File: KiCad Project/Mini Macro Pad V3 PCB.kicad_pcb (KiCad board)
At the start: 2 copper layers, 65 x 65 mm, 59 parts, among them J1 USB_C_Receptacle_USB2.0_14P, SW1 SW_Push bootsel, SW10 SW_Push, SW11 SW_Push, SW12 SW_Push, SW13 SW_Push, SW14 SW_Push, SW15 SW_Push, SW16 SW_Push, SW17 SW_Push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

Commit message: more rough layout
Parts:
- C10, C9: moved to F.Cu
- C7: moved to B.Cu
- moved SW1 59.2 mm to (129.5, 119.0), turned to 180 degrees
- moved R1 52.2 mm to (131.5, 115.3), turned to 90 degrees
- moved C7 15.6 mm to (120.0, 98.4), turned to 0 degrees
- moved C10 14.0 mm to (124.0, 90.0), turned to -90 degrees
- moved Y1 13.8 mm to (119.0, 103.9)
- moved C9 13.6 mm to (118.5, 90.0), turned to 90 degrees
- moved C13 10.6 mm to (122.0, 103.9)
- moved R2 10.4 mm to (119.6, 101.2), turned to 180 degrees
- moved C12 10.3 mm to (116.0, 103.9), turned to -90 degrees
- moved C11 9.64 mm to (116.5, 90.0)
- moved C2 9.64 mm to (113.5, 97.0)
- moved C3 9.64 mm to (124.9, 93.5)
- moved C4 9.64 mm to (113.6, 93.5)
- moved C5 9.64 mm to (124.9, 97.0)
- moved C6 9.64 mm to (119.5, 89.9)
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
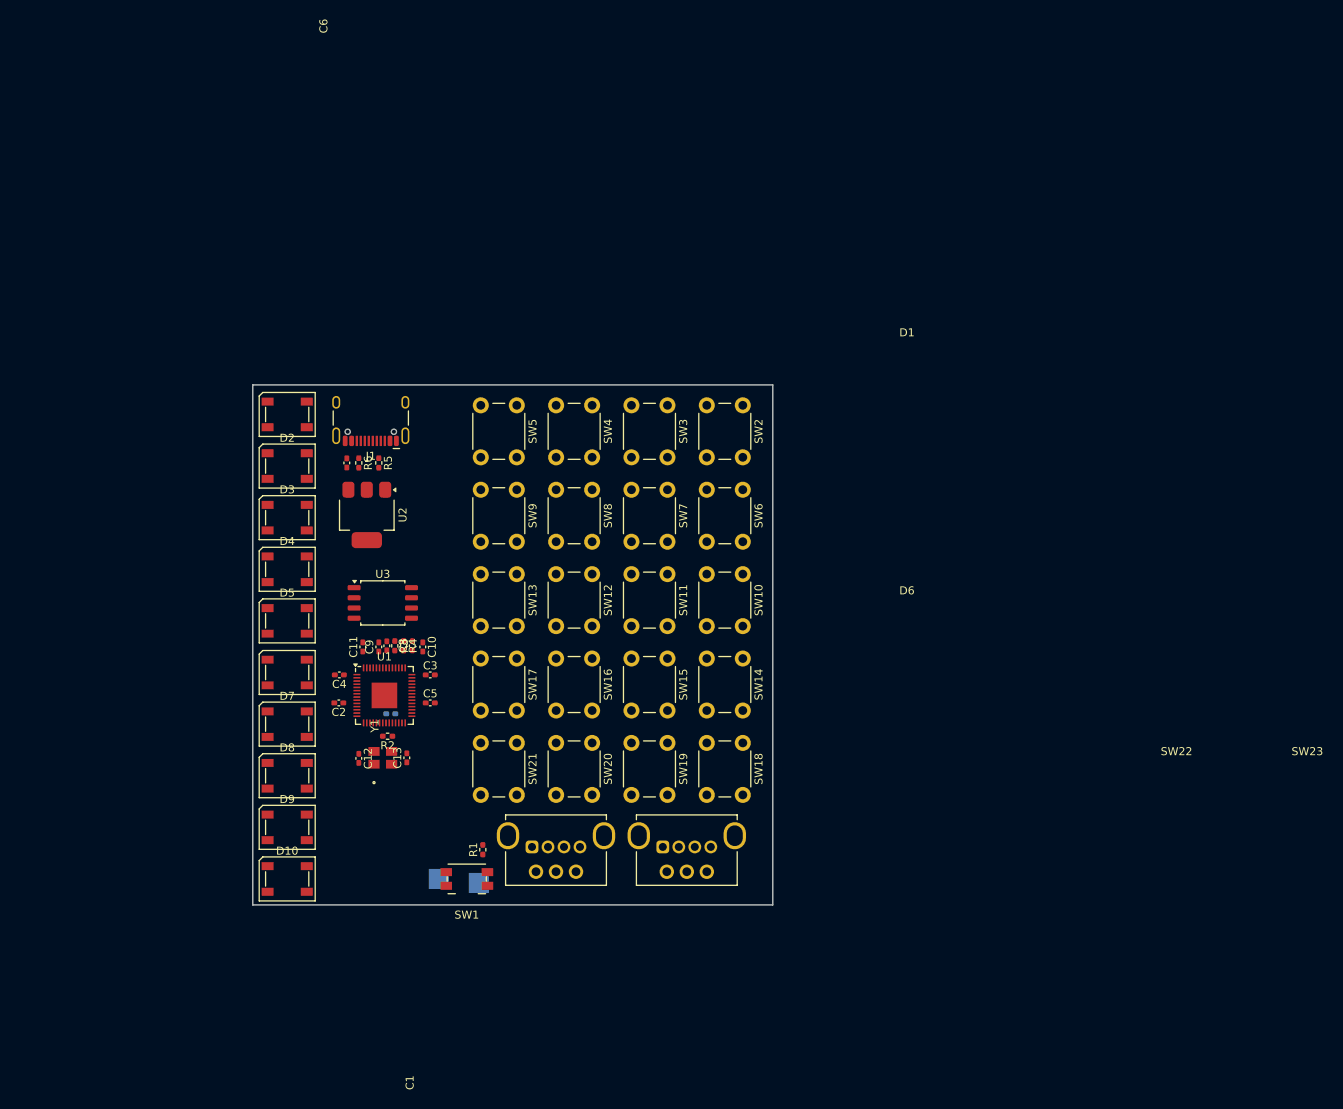
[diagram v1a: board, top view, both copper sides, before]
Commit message: added test points & fixed layout issues with buttons
some buttons were numbered in the wrong order.
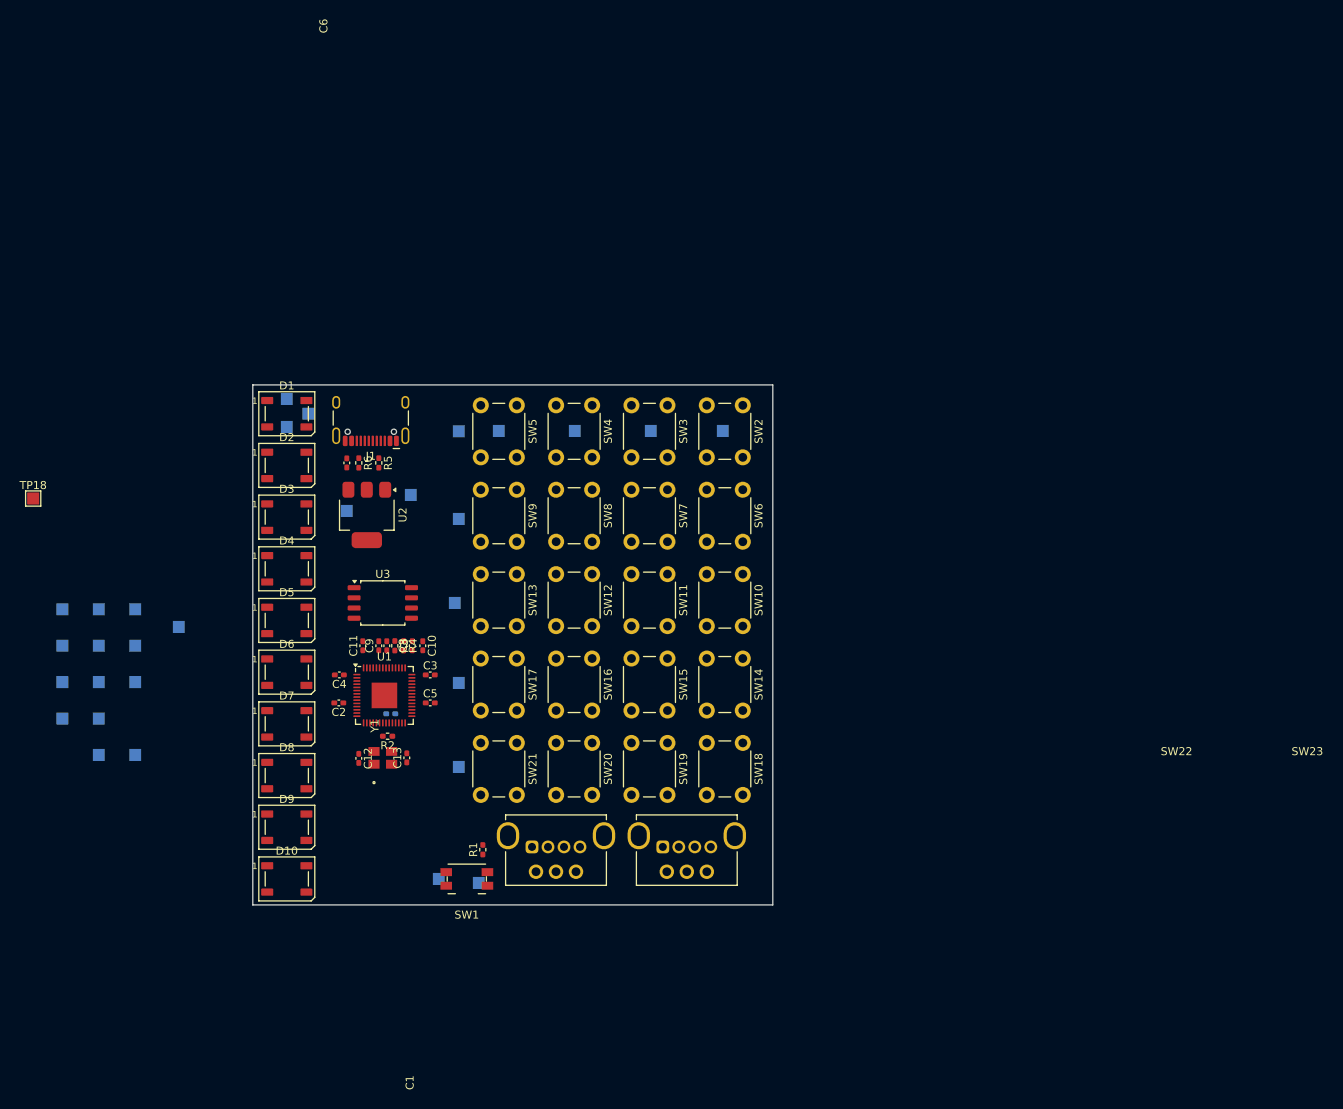
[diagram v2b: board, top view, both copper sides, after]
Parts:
- added TP10: ~, TestPoint:TestPoint_Pad_1.5x1.5mm, B.Cu at (83.5, 94.4)
- added TP11: ~, TestPoint:TestPoint_Pad_1.5x1.5mm, B.Cu at (83.5, 99.0)
- added TP12: ~, TestPoint:TestPoint_Pad_1.5x1.5mm, B.Cu at (83.5, 103.5)
- added TP13: ~, TestPoint:TestPoint_Pad_1.5x1.5mm, B.Cu at (79.0, 85.3)
- added TP14: ~, TestPoint:TestPoint_Pad_1.5x1.5mm, B.Cu at (79.0, 89.8)
- added TP15: ~, TestPoint:TestPoint_Pad_1.5x1.5mm, B.Cu at (79.0, 94.4)
- added TP16: ~, TestPoint:TestPoint_Pad_1.5x1.5mm, B.Cu at (79.0, 99.0)
- added TP17: ~, TestPoint:TestPoint_Pad_1.5x1.5mm, B.Cu at (109.7, 60.9)
- added TP18: ~, TestPoint:TestPoint_Pad_1.5x1.5mm, F.Cu at (75.3, 71.5)
- added TP19: ~, TestPoint:TestPoint_Pad_1.5x1.5mm, B.Cu at (107.0, 62.5)
- added TP20: ~, TestPoint:TestPoint_Pad_1.5x1.5mm, B.Cu at (107.0, 59.0)
- added TP21: ~, TestPoint:TestPoint_Pad_1.5x1.5mm, B.Cu at (122.5, 71.0)
- added TP22: ~, TestPoint:TestPoint_Pad_1.5x1.5mm, B.Cu at (114.5, 73.0)
- added TP23: ~, TestPoint:TestPoint_Pad_1.5x1.5mm, B.Cu at (128.5, 63.0)
- added TP24: ~, TestPoint:TestPoint_Pad_1.5x1.5mm, B.Cu at (128.5, 74.0)
- added TP25: ~, TestPoint:TestPoint_Pad_1.5x1.5mm, B.Cu at (128.0, 84.5)
- added TP26: ~, TestPoint:TestPoint_Pad_1.5x1.5mm, B.Cu at (128.5, 94.5)
- added TP27: ~, TestPoint:TestPoint_Pad_1.5x1.5mm, B.Cu at (128.5, 105.0)
- added TP28: ~, TestPoint:TestPoint_Pad_1.5x1.5mm, B.Cu at (133.5, 63.0)
- added TP29: ~, TestPoint:TestPoint_Pad_1.5x1.5mm, B.Cu at (143.0, 63.0)
- added TP3: ~, TestPoint:TestPoint_Pad_1.5x1.5mm, B.Cu at (88.0, 85.3)
- added TP30: ~, TestPoint:TestPoint_Pad_1.5x1.5mm, B.Cu at (152.5, 63.0)
- added TP31: ~, TestPoint:TestPoint_Pad_1.5x1.5mm, B.Cu at (161.5, 63.0)
- added TP4: ~, TestPoint:TestPoint_Pad_1.5x1.5mm, B.Cu at (88.0, 89.8)
- added TP5: ~, TestPoint:TestPoint_Pad_1.5x1.5mm, B.Cu at (88.0, 94.4)
- added TP6: ~, TestPoint:TestPoint_Pad_1.5x1.5mm, B.Cu at (93.5, 87.5)
- added TP7: ~, TestPoint:TestPoint_Pad_1.5x1.5mm, B.Cu at (88.0, 103.5)
- added TP8: ~, TestPoint:TestPoint_Pad_1.5x1.5mm, B.Cu at (83.5, 85.3)
- added TP9: ~, TestPoint:TestPoint_Pad_1.5x1.5mm, B.Cu at (83.5, 89.8)
- D1, D10, D2, D3, D4, D5, D6, D7, D8, D9: value NeoPixel_THT -> WS2812B; footprint LED_SMD:LED_SK6812_PLCC4_5.0x5.0mm_P3.2mm -> LED_SMD:LED_WS2812B_PLCC4_5.0x5.0mm_P3.2mm
- TP1, TP2: footprint TestPoint:TestPoint_Pad_2.5x2.5mm -> TestPoint:TestPoint_Pad_1.5x1.5mm
- moved C10 0.15 mm to (124.0, 89.9)
- moved C11 0.15 mm to (116.5, 89.9)
- moved C9 0.15 mm to (118.5, 89.9)
- moved D1 0.10 mm to (107.0, 60.9)
- moved D2 0.10 mm to (107.0, 67.3)
- moved D3 0.09 mm to (107.0, 73.8)
- moved D4 0.08 mm to (107.0, 80.2)
- moved D5 0.07 mm to (107.0, 86.7)
- moved D6 0.07 mm to (107.0, 93.2)
- moved D7 0.06 mm to (107.0, 99.6)
- moved D8 0.05 mm to (107.0, 106.1)
- moved D9 0.05 mm to (107.0, 112.5)
- moved D10 0.05 mm to (107.0, 119.0)
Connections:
- D1 pad 1: Net-(D1-DOUT) -> +3.3V
- D1 pad 2: GND -> Net-(D1-DOUT)
- D1 pad 3: +3.3V -> GND
- D10 pad 1: Net-(D10-DOUT) -> +3.3V
- D10 pad 2: GND -> unconnected-(D10-DOUT-Pad2)
- D10 pad 3: +3.3V -> GND
- D2 pad 1: Net-(D2-DOUT) -> +3.3V
- D2 pad 2: GND -> Net-(D2-DOUT)
- D2 pad 3: +3.3V -> GND
- D3 pad 1: Net-(D3-DOUT) -> +3.3V
- D3 pad 2: GND -> Net-(D3-DOUT)
- D3 pad 3: +3.3V -> GND
- D4 pad 1: Net-(D4-DOUT) -> +3.3V
- D4 pad 2: GND -> Net-(D4-DOUT)
- D4 pad 3: +3.3V -> GND
- D5 pad 1: Net-(D5-DOUT) -> +3.3V
- D5 pad 2: GND -> Net-(D5-DOUT)
- D5 pad 3: +3.3V -> GND
- D6 pad 1: Net-(D10-DIN) -> +3.3V
- D6 pad 2: GND -> Net-(D6-DOUT)
- D6 pad 3: +3.3V -> GND
- D7 pad 1: Net-(D7-DOUT) -> +3.3V
- D7 pad 2: GND -> Net-(D7-DOUT)
- D7 pad 3: +3.3V -> GND
- D7 pad 4: Net-(D10-DOUT) -> Net-(D6-DOUT)
- D8 pad 1: Net-(D8-DOUT) -> +3.3V
- D8 pad 2: GND -> Net-(D8-DOUT)
- D8 pad 3: +3.3V -> GND
- D9 pad 1: unconnected-(D9-DOUT-Pad1) -> +3.3V
- D9 pad 2: GND -> Net-(D10-DIN)
- D9 pad 3: +3.3V -> GND
- SW11 pad 1: /MATRIX_C1 -> /MATRIX_C2
- SW11 pad 2: /MATRIX_R4 -> /MATRIX_R3
- SW12 pad 1: /MATRIX_C2 -> /MATRIX_C3
- SW13 pad 1: /MATRIX_C2 -> /MATRIX_C4
- SW13 pad 2: /MATRIX_R4 -> /MATRIX_R3
- SW14 pad 1: /MATRIX_C3 -> /MATRIX_C1
- SW14 pad 2: /MATRIX_R3 -> /MATRIX_R4
- SW15 pad 1: /MATRIX_C3 -> /MATRIX_C2
- SW16 pad 1: /MATRIX_C4 -> /MATRIX_C3
- SW16 pad 2: /MATRIX_R3 -> /MATRIX_R4
- U1 pad 27: unconnected-(U1-GPIO16-Pad27) -> Net-(U1-GPIO16)
- U1 pad 28: unconnected-(U1-GPIO17-Pad28) -> Net-(U1-GPIO17)
- U1 pad 29: unconnected-(U1-GPIO18-Pad29) -> Net-(U1-GPIO18)
- U1 pad 30: unconnected-(U1-GPIO19-Pad30) -> Net-(U1-GPIO19)
- U1 pad 31: unconnected-(U1-GPIO20-Pad31) -> Net-(U1-GPIO20)
- U1 pad 32: unconnected-(U1-GPIO21-Pad32) -> Net-(U1-GPIO21)
- U1 pad 34: unconnected-(U1-GPIO22-Pad34) -> Net-(U1-GPIO22)
- U1 pad 35: unconnected-(U1-GPIO23-Pad35) -> Net-(U1-GPIO23)
- U1 pad 36: unconnected-(U1-GPIO24-Pad36) -> Net-(U1-GPIO24)
- U1 pad 37: unconnected-(U1-GPIO25-Pad37) -> Net-(U1-GPIO25)
- U1 pad 38: unconnected-(U1-GPIO26_ADC0-Pad38) -> Net-(U1-GPIO26_ADC0)
- U1 pad 39: unconnected-(U1-GPIO27_ADC1-Pad39) -> Net-(U1-GPIO27_ADC1)
- U1 pad 40: unconnected-(U1-GPIO28_ADC2-Pad40) -> Net-(U1-GPIO28_ADC2)
- U1 pad 41: unconnected-(U1-GPIO29_ADC3-Pad41) -> Net-(U1-GPIO29_ADC3)

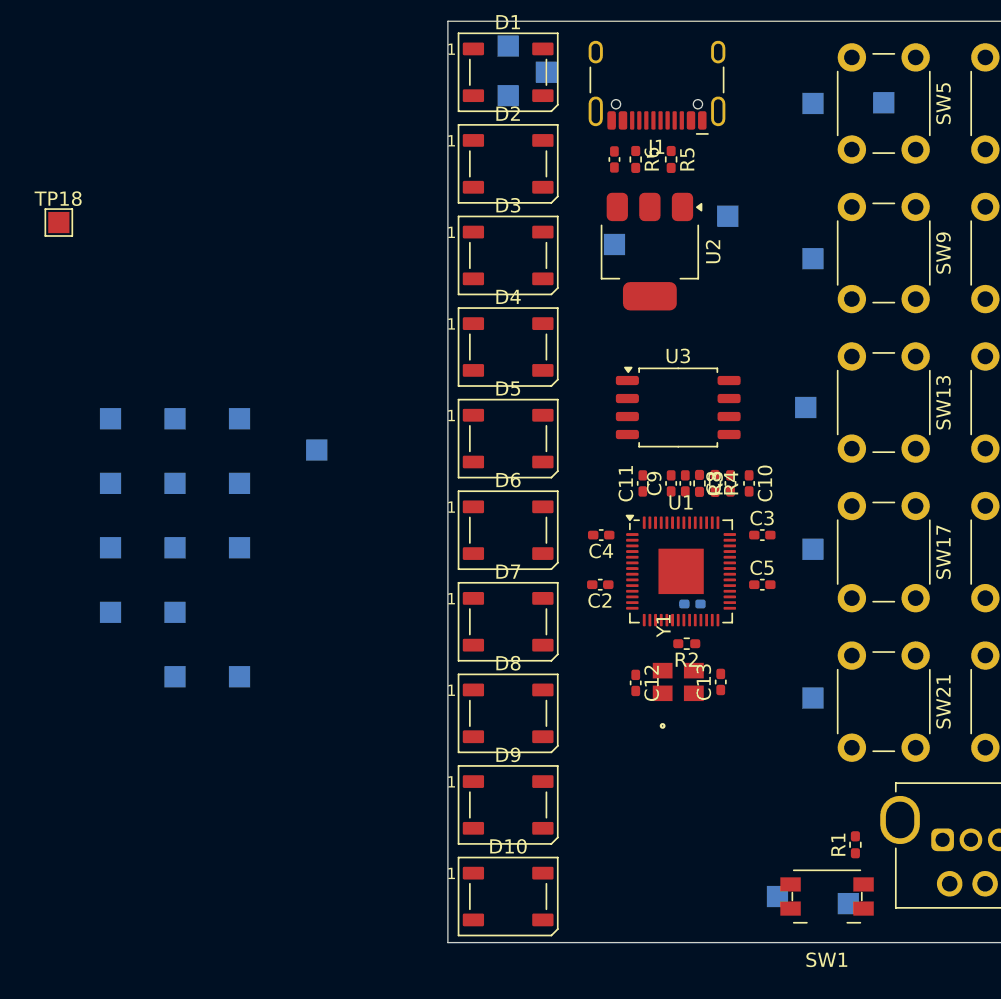
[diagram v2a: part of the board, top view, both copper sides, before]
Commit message: changed GPIO pins used
moved rotary encoder GPIO pins away from the pins used for the crystal to prevent stability issues
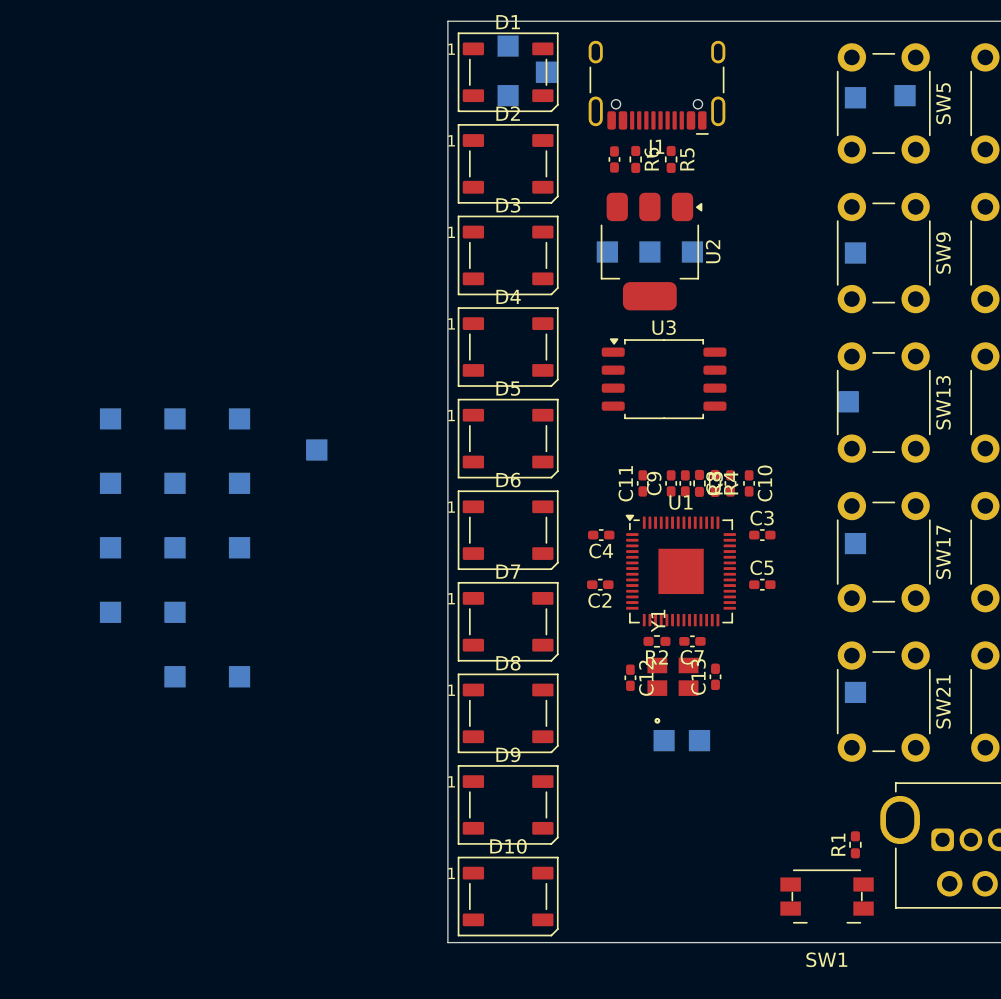
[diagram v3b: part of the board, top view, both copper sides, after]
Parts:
- C7: moved to F.Cu
- TP18: moved to B.Cu
- moved TP18 34.1 mm to (107.0, 59.0), turned to 180 degrees
- moved TP20 17.6 mm to (117.0, 73.5)
- moved TP2 15.6 mm to (120.5, 108.0)
- moved TP1 13.6 mm to (118.0, 108.0)
- moved TP21 3.56 mm to (120.0, 73.5)
- moved TP24 3.03 mm to (131.5, 73.6)
- moved TP25 3.03 mm to (131.0, 84.1)
- moved TP26 3.03 mm to (131.5, 94.1)
- moved TP27 3.03 mm to (131.5, 104.6)
- moved TP23 3.03 mm to (131.5, 62.6)
- moved C7 2.64 mm to (120.0, 101.0), turned to 180 degrees
- moved U3 2.24 mm to (118.0, 82.5)
- moved R2 2.11 mm to (117.5, 101.0)
- moved TP28 1.58 mm to (135.0, 62.5)
- moved TP22 0.73 mm to (114.0, 73.5)
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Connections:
- TP10 pad 1: Net-(U1-GPIO23) -> Net-(U1-GPIO17)
- TP11 pad 1: Net-(U1-GPIO24) -> Net-(U1-GPIO18)
- TP12 pad 1: Net-(U1-GPIO25) -> Net-(U1-GPIO19)
- TP3 pad 1: Net-(U1-GPIO16) -> Net-(U1-GPIO10)
- TP4 pad 1: Net-(U1-GPIO17) -> Net-(U1-GPIO11)
- TP5 pad 1: Net-(U1-GPIO18) -> Net-(U1-GPIO12)
- TP6 pad 1: Net-(U1-GPIO19) -> Net-(U1-GPIO13)
- TP7 pad 1: Net-(U1-GPIO20) -> Net-(U1-GPIO14)
- TP8 pad 1: Net-(U1-GPIO21) -> Net-(U1-GPIO15)
- TP9 pad 1: Net-(U1-GPIO22) -> Net-(U1-GPIO16)
- U1 pad 13: /ENCODER_1_A -> Net-(U1-GPIO10)
- U1 pad 14: /ENCODER_1_B -> Net-(U1-GPIO11)
- U1 pad 15: /ENCODER_1_S1 -> Net-(U1-GPIO12)
- U1 pad 16: /ENCODER_2_A -> Net-(U1-GPIO13)
- U1 pad 17: /ENCODER_2_B -> Net-(U1-GPIO14)
- U1 pad 18: /ENCODER_2_S1 -> Net-(U1-GPIO15)
- U1 pad 31: Net-(U1-GPIO20) -> /ENCODER_1_A
- U1 pad 32: Net-(U1-GPIO21) -> /ENCODER_1_B
- U1 pad 34: Net-(U1-GPIO22) -> /ENCODER_1_S1
- U1 pad 35: Net-(U1-GPIO23) -> /ENCODER_2_A
- U1 pad 36: Net-(U1-GPIO24) -> /ENCODER_2_B
- U1 pad 37: Net-(U1-GPIO25) -> /ENCODER_2_S1
